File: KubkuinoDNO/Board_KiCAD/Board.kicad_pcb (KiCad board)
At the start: 2 copper layers, 37 parts, among them J1 Piezo, J2 AC In (12V), J3 Prog, J4 Czujnik, J6 LCD, J7 Button, J8 Bluetooth, J9 1wire, Q1 S8050, SW1 Reset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

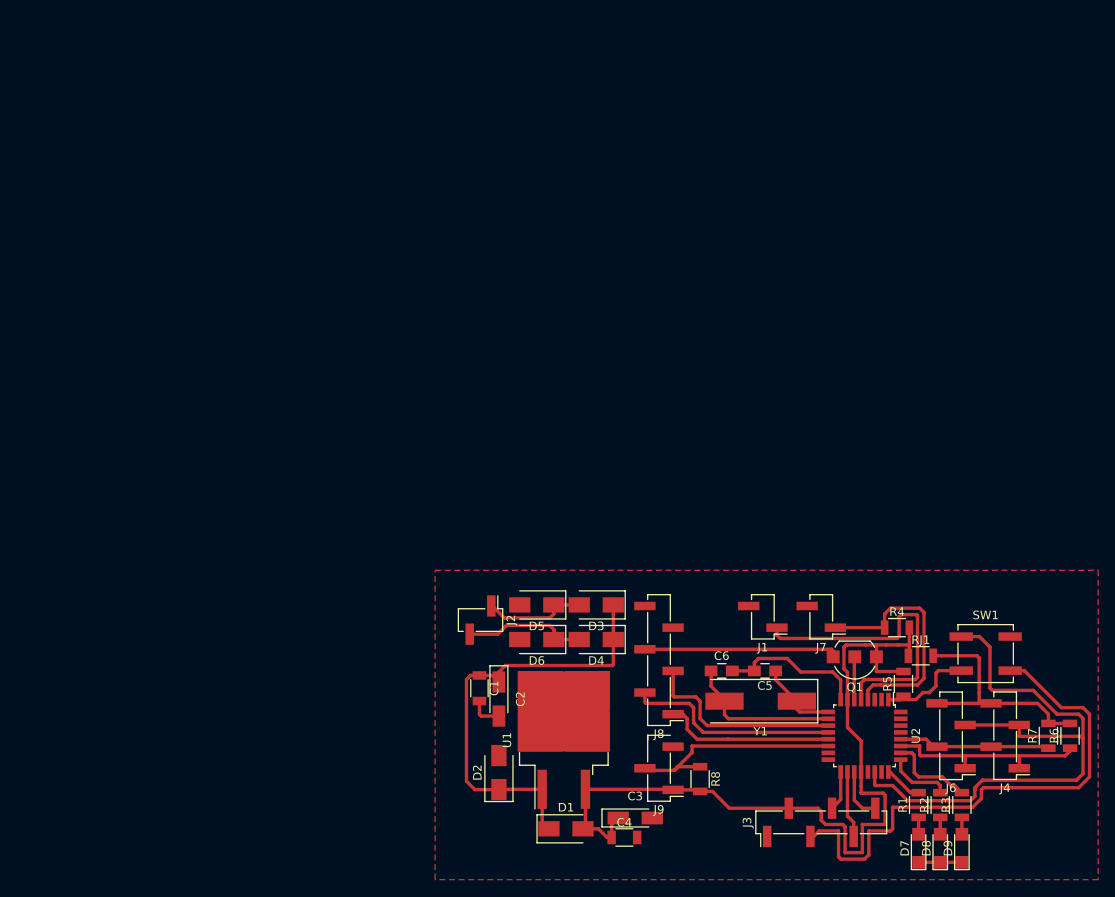
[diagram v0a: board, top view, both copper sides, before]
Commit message: Upgrades
Aktualizacja głównego kodu do użycia czujnika podczerwonego
Ukończenie płytki (SMD)
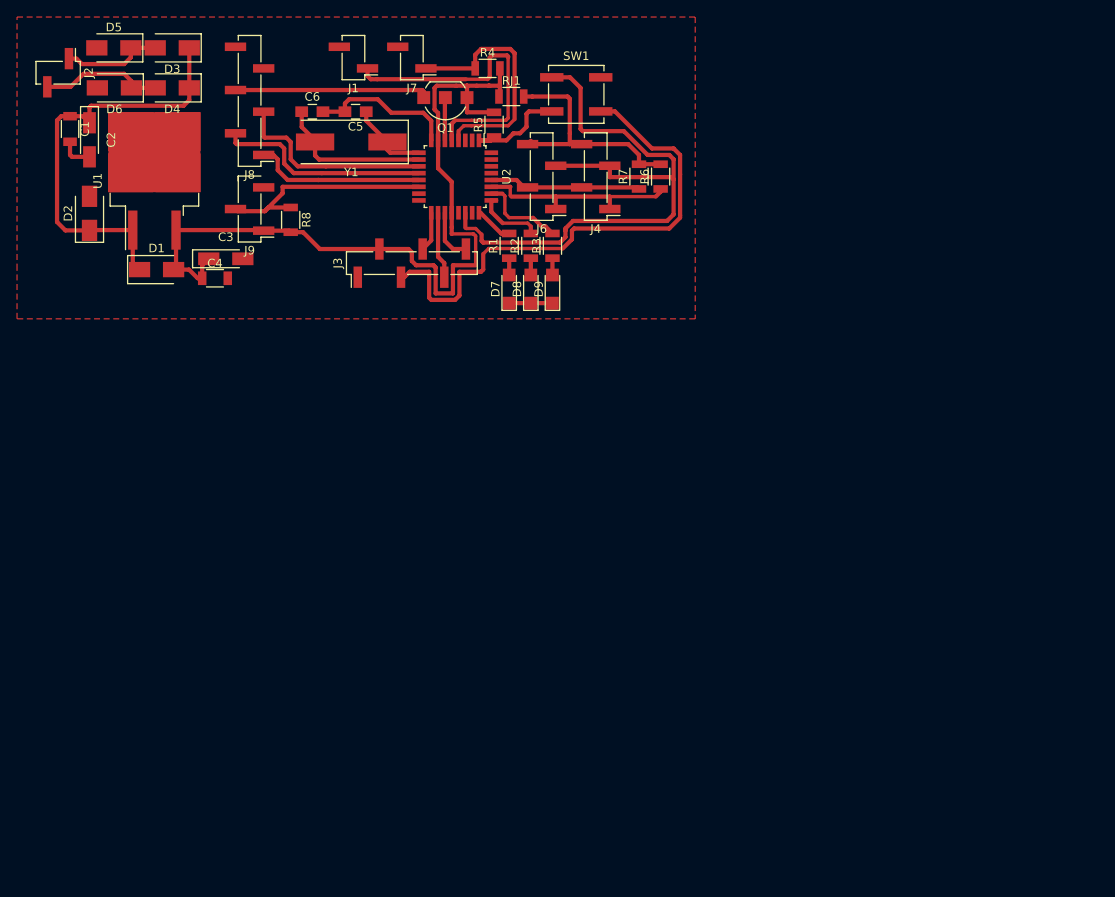
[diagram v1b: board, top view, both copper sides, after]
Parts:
- moved D3 82.2 mm to (76.2, 52.6)
- moved D5 82.1 mm to (69.3, 52.6)
- moved D4 81.7 mm to (76.2, 57.3)
- moved D6 81.6 mm to (69.4, 57.3)
- moved C2 81.4 mm to (66.5, 63.4)
- moved R1 81.4 mm to (115.8, 75.8)
- moved C3 81.4 mm to (82.5, 77.3)
- moved C4 81.4 mm to (81.2, 79.6)
- moved C6 81.4 mm to (92.6, 60.1)
- moved D2 81.4 mm to (66.5, 72.0)
- moved R2 81.4 mm to (118.3, 75.8)
- moved U1 81.4 mm to (74.1, 68.2)
- moved C1 81.4 mm to (64.2, 62.1)
- moved C5 81.4 mm to (97.7, 60.1)
- moved D7 81.4 mm to (115.8, 80.9)
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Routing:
- net Net-(C1-Pad1): track 53.6 -> 51.6 mm
- net Net-(D4-Pad2): track 15.2 -> 14.5 mm
- net GND: track 98.8 -> 99.5 mm
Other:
- net class Default: trace_width 0.4 -> 0.5
